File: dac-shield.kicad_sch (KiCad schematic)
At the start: 39 parts, among them J1 Conn_01x02, J2 Conn_01x02, J3 Conn_01x02, J4 Conn_01x02, J5 Conn_01x02, J6 Conn_01x02, J7 Conn_01x02, J8 Conn_01x02

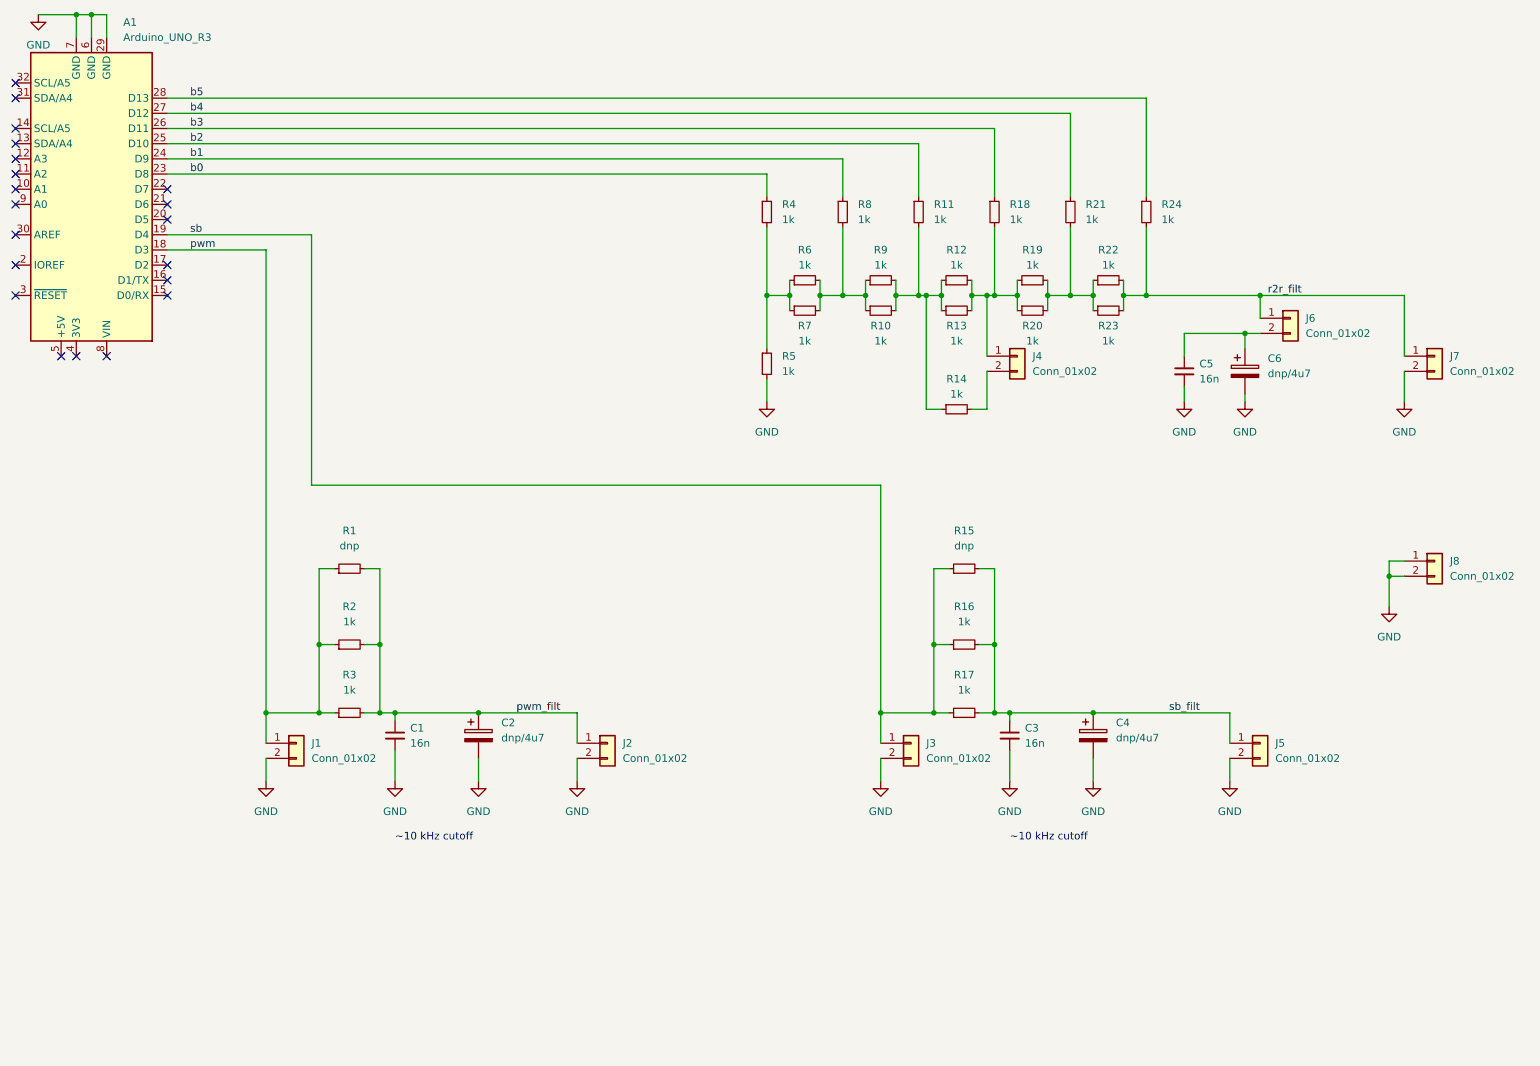
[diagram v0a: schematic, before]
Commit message: fixed cap value and added annotations
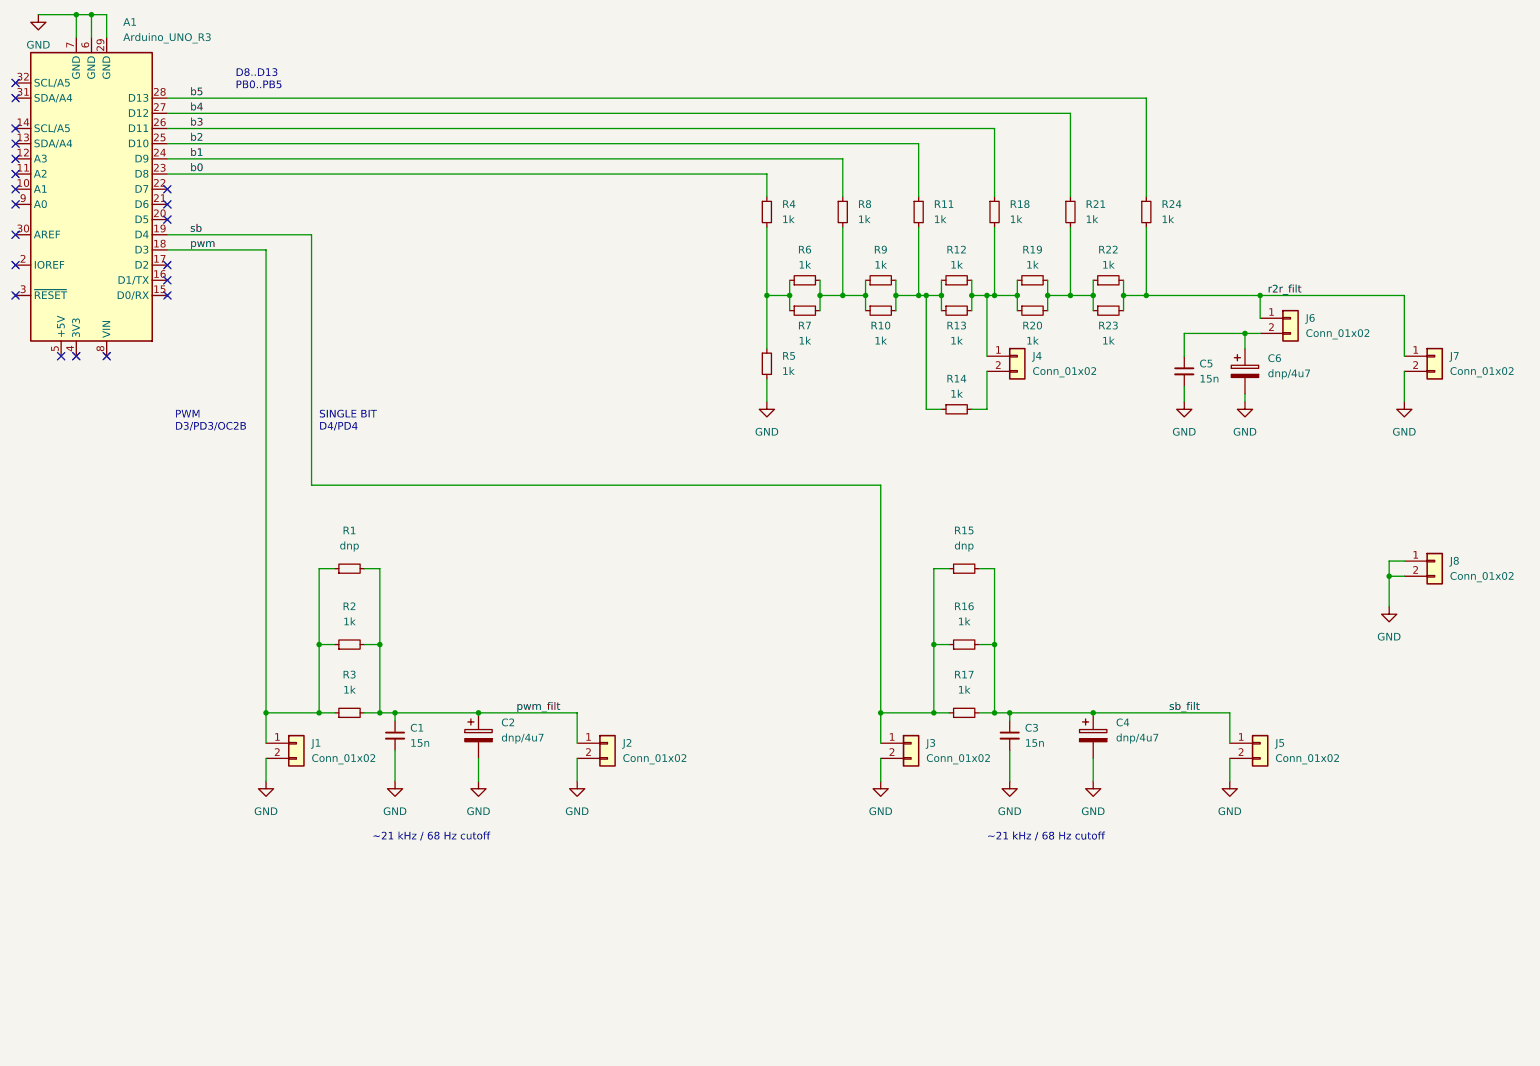
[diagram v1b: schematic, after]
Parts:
- C1, C3, C5: value 16n -> 15n
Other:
- note added: "D8..D13 PB0..PB5"
- note added: "PWM D3/PD3/OC2B"
- note added: "SINGLE BIT D4/PD4"
- note added: "~21 kHz / 68 Hz cutoff"
- note removed: "~10 kHz cutoff"
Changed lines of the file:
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@@
     (stroke (width 0) (type default) (color 0 0 0 0))
   )
-  (text "~10 kHz cutoff" (at 81.28 154.94 0)
-    (effects (font (size 1.27 1.27)) (justify left bottom))
-  )
-  (text "~10 kHz cutoff" (at 184.15 154.94 0)
+  (text "D8..D13\nPB0..PB5" (at 54.61 29.21 0)
+    (effects (font (size 1.27 1.27)) (justify left bottom))
+  )
+  (text "PWM\nD3/PD3/OC2B" (at 44.45 86.36 0)
+    (effects (font (size 1.27 1.27)) (justify left bottom))
+  )
+  (text "~21 kHz / 68 Hz cutoff" (at 77.47 154.94 0)
+    (effects (font (size 1.27 1.27)) (justify left bottom))
+  )
+  (text "~21 kHz / 68 Hz cutoff" (at 180.34 154.94 0)
+    (effects (font (size 1.27 1.27)) (justify left bottom))
+  )
+  (text "SINGLE BIT\nD4/PD4" (at 68.58 86.36 0)
     (effects (font (size 1.27 1.27)) (justify left bottom))
   )
@@
       (effects (font (size 1.27 1.27)) (justify left))
     )
-    (property "Value" "16n" (id 1) (at 215.9 77.4762 0)
+    (property "Value" "15n" (id 1) (at 215.9 77.4762 0)
       (effects (font (size 1.27 1.27)) (justify left))
     )
@@
       (effects (font (size 1.27 1.27)) (justify left))
     )
-    (property "Value" "16n" (id 1) (at 186.69 138.4362 0)
+    (property "Value" "15n" (id 1) (at 186.69 138.4362 0)
       (effects (font (size 1.27 1.27)) (justify left))
     )
@@
       (effects (font (size 1.27 1.27)) (justify left))
     )
-    (property "Value" "16n" (id 1) (at 83.82 138.4362 0)
+    (property "Value" "15n" (id 1) (at 83.82 138.4362 0)
       (effects (font (size 1.27 1.27)) (justify left))
     )
@@
     )
     (path "/71439bbb-0178-4c31-b619-3a3597f26a66"
-      (reference "C1") (unit 1) (value "16n") (footprint "Capacitor_SMD:C_0603_1608Metric")
+      (reference "C1") (unit 1) (value "15n") (footprint "Capacitor_SMD:C_0603_1608Metric")
     )
     (path "/175a1dee-16dc-4331-a44f-fe26d859c713"
@@
     )
     (path "/6c811e9f-a68c-442b-9221-df5c63574d14"
-      (reference "C3") (unit 1) (value "16n") (footprint "Capacitor_SMD:C_0603_1608Metric")
+      (reference "C3") (unit 1) (value "15n") (footprint "Capacitor_SMD:C_0603_1608Metric")
     )
     (path "/c5fed54c-8f94-4496-b282-fd5a5f8d0e35"
@@
     )
     (path "/0cd07eda-f25d-4d63-ba12-ea43f627f074"
-      (reference "C5") (unit 1) (value "16n") (footprint "Capacitor_SMD:C_0603_1608Metric")
+      (reference "C5") (unit 1) (value "15n") (footprint "Capacitor_SMD:C_0603_1608Metric")
     )
     (path "/6c22366a-92ab-4f1f-b457-234a7b84c9ee"

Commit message: added analog feedback
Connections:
- net pwm: now also A1.13 (SDA/A4)
- net pwm_filt: now also A1.12 (A3)
- net r2r_filt: now also A1.9 (A0)
- net sb: now also A1.11 (A2)
- net sb_filt: now also A1.10 (A1)
- no-connect marks 20 -> 15
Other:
- moved on the sheet: A1, C1, C2, C3, C4, C5, C6, J1, J2, J3, J4, J5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

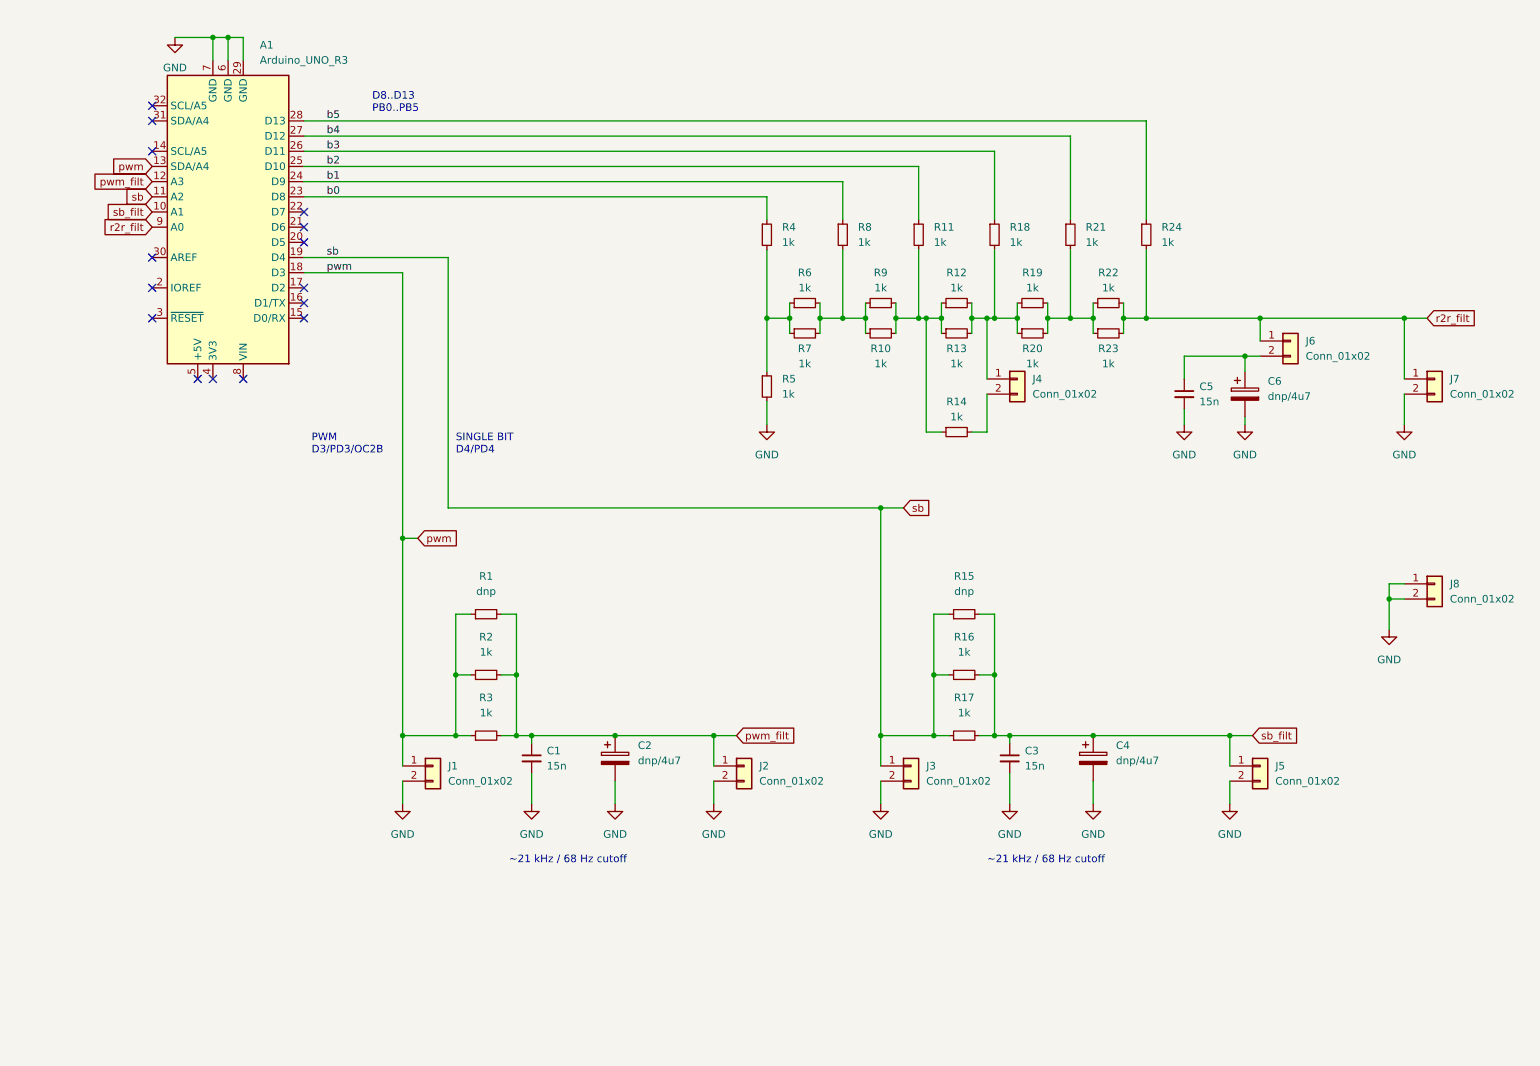
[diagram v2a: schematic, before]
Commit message: added test points, recreated fab files
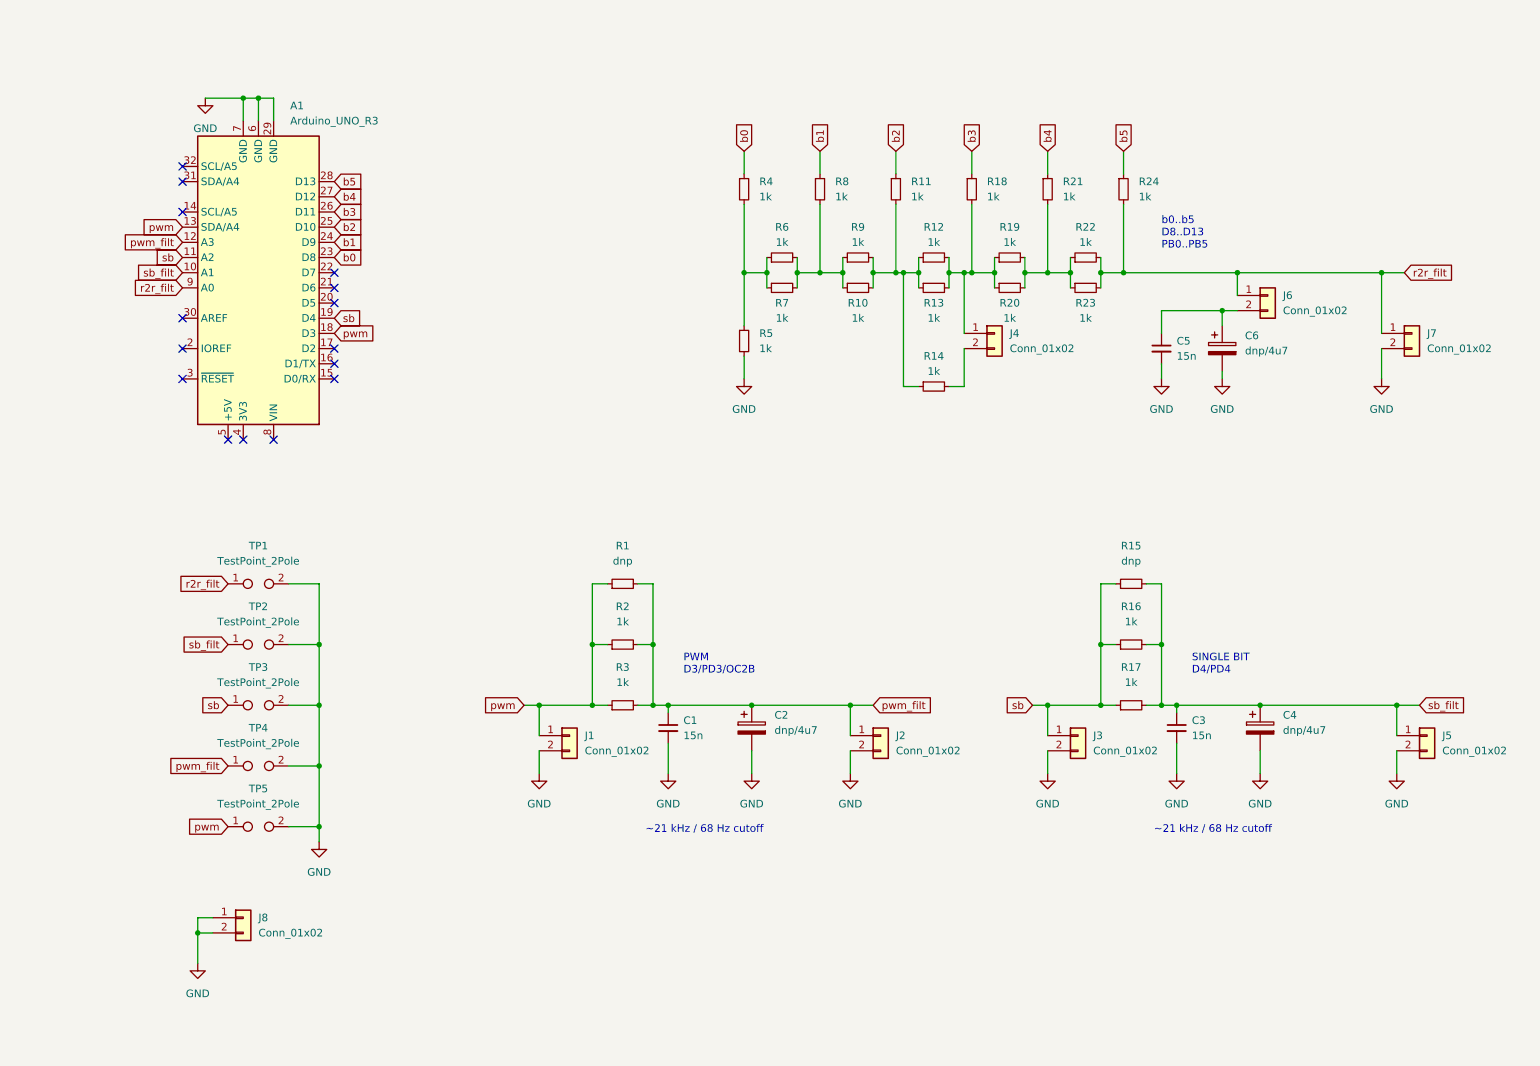
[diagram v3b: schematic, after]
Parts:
- added TP1, TP2, TP3, TP4, TP5: TestPoint_2Pole, TestPoint:TestPoint_2Pads_Pitch2.54mm_Drill0.8mm, symbol Connector:TestPoint_2Pole
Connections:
- net GND: now also TP1.2, TP2.2, TP3.2, TP4.2, TP5.2
- net pwm: now also TP5.1
- net pwm_filt: now also TP4.1
- net r2r_filt: now also TP1.1
- net sb: now also TP3.1
- net sb_filt: now also TP2.1
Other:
- note added: "b0..b5 D8..D13 PB0..PB5"
- note removed: "D8..D13 PB0..PB5"
- moved on the sheet: A1, C1, C2, C3, C4, C5, C6, J1, J2, J3, J4, J5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

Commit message: prettified things
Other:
- note added: "ARDUINO UNO"
- note added: "PWM DAC"
- note added: "R2R DAC"
- note added: "SINGLE BIT DAC"
- note added: "TEST POINTS"
- moved on the sheet: A1, C1, C2, C3, C4, C5, C6, J1, J2, J3, J4, J5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

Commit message: changed testpoint footprints
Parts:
- TP1, TP2, TP3, TP4, TP5: footprint TestPoint:TestPoint_2Pads_Pitch2.54mm_Drill0.8mm -> Connector_PinHeader_2.54mm:PinHeader_1x02_P2.54mm_Vertical
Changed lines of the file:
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@@
     (property "Reference" "TP2" (id 0) (at 53.34 119.38 0))
     (property "Value" "TestPoint_2Pole" (id 1) (at 53.34 121.92 0))
-    (property "Footprint" "TestPoint:TestPoint_2Pads_Pitch2.54mm_Drill0.8mm" (id 2) (at 53.34 125.73 0)
+    (property "Footprint" "Connector_PinHeader_2.54mm:PinHeader_1x02_P2.54mm_Vertical" (id 2) (at 53.34 125.73 0)
       (effects (font (size 1.27 1.27)) hide)
     )
@@
     (property "Reference" "TP5" (id 0) (at 53.34 149.86 0))
     (property "Value" "TestPoint_2Pole" (id 1) (at 53.34 152.4 0))
-    (property "Footprint" "TestPoint:TestPoint_2Pads_Pitch2.54mm_Drill0.8mm" (id 2) (at 53.34 156.21 0)
+    (property "Footprint" "Connector_PinHeader_2.54mm:PinHeader_1x02_P2.54mm_Vertical" (id 2) (at 53.34 156.21 0)
       (effects (font (size 1.27 1.27)) hide)
     )
@@
     (property "Reference" "TP1" (id 0) (at 53.34 109.22 0))
     (property "Value" "TestPoint_2Pole" (id 1) (at 53.34 111.76 0))
-    (property "Footprint" "TestPoint:TestPoint_2Pads_Pitch2.54mm_Drill0.8mm" (id 2) (at 53.34 115.57 0)
+    (property "Footprint" "Connector_PinHeader_2.54mm:PinHeader_1x02_P2.54mm_Vertical" (id 2) (at 53.34 115.57 0)
       (effects (font (size 1.27 1.27)) hide)
     )
@@
     (property "Reference" "TP4" (id 0) (at 53.34 139.7 0))
     (property "Value" "TestPoint_2Pole" (id 1) (at 53.34 142.24 0))
-    (property "Footprint" "TestPoint:TestPoint_2Pads_Pitch2.54mm_Drill0.8mm" (id 2) (at 53.34 146.05 0)
+    (property "Footprint" "Connector_PinHeader_2.54mm:PinHeader_1x02_P2.54mm_Vertical" (id 2) (at 53.34 146.05 0)
       (effects (font (size 1.27 1.27)) hide)
     )
@@
     (property "Reference" "TP3" (id 0) (at 53.34 129.54 0))
     (property "Value" "TestPoint_2Pole" (id 1) (at 53.34 132.08 0))
-    (property "Footprint" "TestPoint:TestPoint_2Pads_Pitch2.54mm_Drill0.8mm" (id 2) (at 53.34 135.89 0)
+    (property "Footprint" "Connector_PinHeader_2.54mm:PinHeader_1x02_P2.54mm_Vertical" (id 2) (at 53.34 135.89 0)
       (effects (font (size 1.27 1.27)) hide)
     )
@@
     )
     (path "/5c667e6e-f8ce-42a6-9e4a-18a160bf0f06"
-      (reference "TP1") (unit 1) (value "TestPoint_2Pole") (footprint "TestPoint:TestPoint_2Pads_Pitch2.54mm_Drill0.8mm")
+      (reference "TP1") (unit 1) (value "TestPoint_2Pole") (footprint "Connector_PinHeader_2.54mm:PinHeader_1x02_P2.54mm_Vertical")
     )
     (path "/34476816-0ae8-46ae-a952-81cb362d8b82"
-      (reference "TP2") (unit 1) (value "TestPoint_2Pole") (footprint "TestPoint:TestPoint_2Pads_Pitch2.54mm_Drill0.8mm")
+      (reference "TP2") (unit 1) (value "TestPoint_2Pole") (footprint "Connector_PinHeader_2.54mm:PinHeader_1x02_P2.54mm_Vertical")
     )
     (path "/f88d20cf-bb43-4c36-8270-9ba485a67579"
-      (reference "TP3") (unit 1) (value "TestPoint_2Pole") (footprint "TestPoint:TestPoint_2Pads_Pitch2.54mm_Drill0.8mm")
+      (reference "TP3") (unit 1) (value "TestPoint_2Pole") (footprint "Connector_PinHeader_2.54mm:PinHeader_1x02_P2.54mm_Vertical")
     )
     (path "/a1626f61-63d5-408a-8b4c-b6ebac3467f0"
-      (reference "TP4") (unit 1) (value "TestPoint_2Pole") (footprint "TestPoint:TestPoint_2Pads_Pitch2.54mm_Drill0.8mm")
+      (reference "TP4") (unit 1) (value "TestPoint_2Pole") (footprint "Connector_PinHeader_2.54mm:PinHeader_1x02_P2.54mm_Vertical")
     )
     (path "/582f8559-feeb-412f-b71f-59739cb91a9b"
-      (reference "TP5") (unit 1) (value "TestPoint_2Pole") (footprint "TestPoint:TestPoint_2Pads_Pitch2.54mm_Drill0.8mm")
-    )
-  )
+      (reference "TP5") (unit 1) (value "TestPoint_2Pole") (footprint "Connector_PinHeader_2.54mm:PinHeader_1x02_P2.54mm_Vertical")
+    )
+  )

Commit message: created footprint options
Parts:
- added C3, C7, C9: dnp/4u7, Capacitor_THT:CP_Radial_D5.0mm_P2.50mm, symbol Device:C_Polarized
- renumbered C5 to C4, C6 to C5, C3 to C6, C4 to C8, J8 to J1, J1 to J2, J2 to J3, J3 to J5, J5 to J8, R18 to R15, R19 to R16, R20 to R17, R21 to R18, R22 to R19, R23 to R20, R24 to R21, R15 to R22, R16 to R23, R17 to R24
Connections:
- net GND: now also C3.2, C7.2, C9.2
- net pwm_filt: now also C3.1
- net sb_filt: now also C9.1
- net at C4.1, C5.1, J6.2 (Pin_2): now also C7.1
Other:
- moved on the sheet: C4, C5, J4, J6, R10, R11, R12, R13, R14, R15, R16, R17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
